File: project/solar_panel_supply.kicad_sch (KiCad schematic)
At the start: 17 parts, among them U1 LT3652EMSE

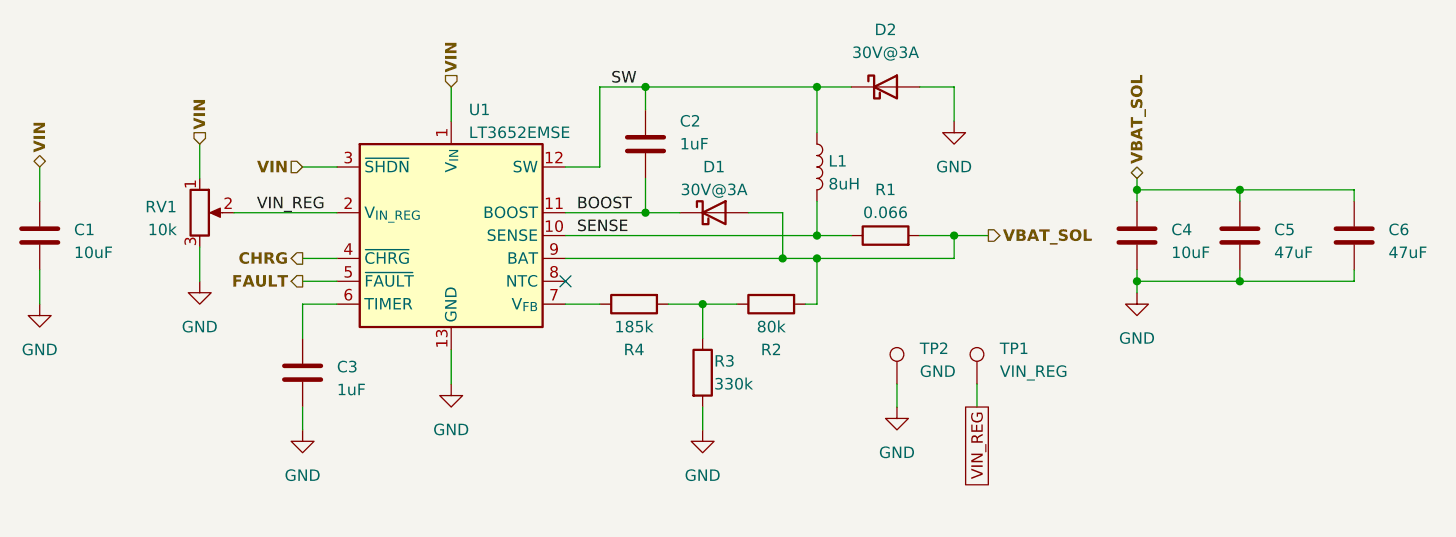
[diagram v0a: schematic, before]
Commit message: Added symbol annotations
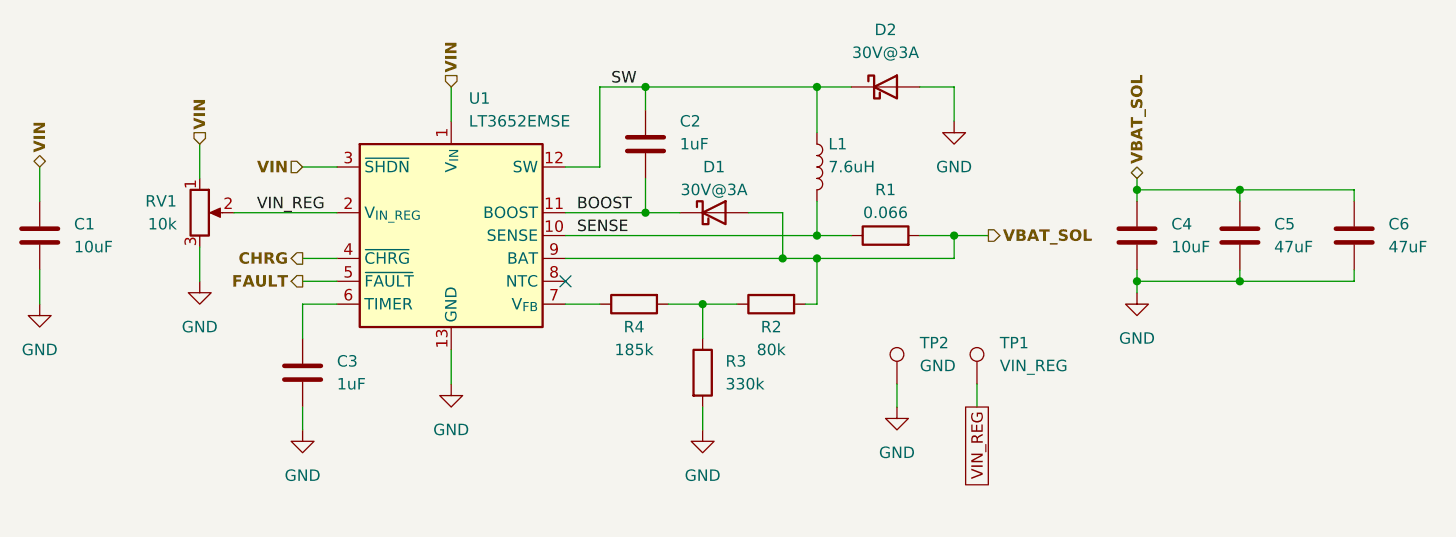
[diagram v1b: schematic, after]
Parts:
- L1: value 8uH -> 7.6uH

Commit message: Added footprints
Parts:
- L1: footprint Inductor_SMD:L_Abracon_ASPI-4030S -> Inductor_SMD:L_Bourns-SRN6028
- RV1: footprint PicoUPS:Potentiometer_Bourns_3214G_Horizontal -> PicoUPS:Potentiometer_Bourns_3313J-1_Vertical
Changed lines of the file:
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@@
       (effects (font (size 1.27 1.27)) (justify left))
     )
-    (property "Footprint" "Inductor_SMD:L_Abracon_ASPI-4030S" (at 166.37 88.9 0)
+    (property "Footprint" "Inductor_SMD:L_Bourns-SRN6028" (at 166.37 88.9 0)
       (effects (font (size 1.27 1.27)) hide)
     )
@@
       (effects (font (size 1.27 1.27)) (justify right))
     )
-    (property "Footprint" "PicoUPS:Potentiometer_Bourns_3214G_Horizontal" (at 97.79 93.98 0)
+    (property "Footprint" "PicoUPS:Potentiometer_Bourns_3313J-1_Vertical" (at 97.79 93.98 0)
       (effects (font (size 1.27 1.27)) hide)
     )

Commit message: Changed to thermal vias footprint
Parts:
- U1: footprint Package_SO:MSOP-12-1EP_3x4mm_P0.65mm_EP1.65x2.85mm -> Package_SO:MSOP-12-1EP_3x4mm_P0.65mm_EP1.65x2.85mm_ThermalVias
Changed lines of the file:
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@@
       (effects (font (size 1.27 1.27)) (justify left))
     )
-    (property "Footprint" "Package_SO:MSOP-12-1EP_3x4mm_P0.65mm_EP1.65x2.85mm" (at 125.73 111.76 0)
+    (property "Footprint" "Package_SO:MSOP-12-1EP_3x4mm_P0.65mm_EP1.65x2.85mm_ThermalVias" (at 125.73 111.76 0)
       (effects (font (size 1.27 1.27)) hide)
     )

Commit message: Final revision
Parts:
- renumbered C4 to C2, C5 to C3, C6 to C4, C2 to C5, C3 to C6, D2 to D1, D1 to D2, R4 to R3, R3 to R4
